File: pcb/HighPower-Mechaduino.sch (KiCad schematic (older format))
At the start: 55 parts, among them J1 SUPPLY, J2 STEPPER, P1 SWD, P4 -, P5 -, P6 -, P7 -, Q1 SSM3J328R, Q2 BSS138, SW1 B3U-1000P, U1 AS5047D, U2 AP2112K-3.3TRG1, U3 AT24CS64-SSHM, U9 LM75BD

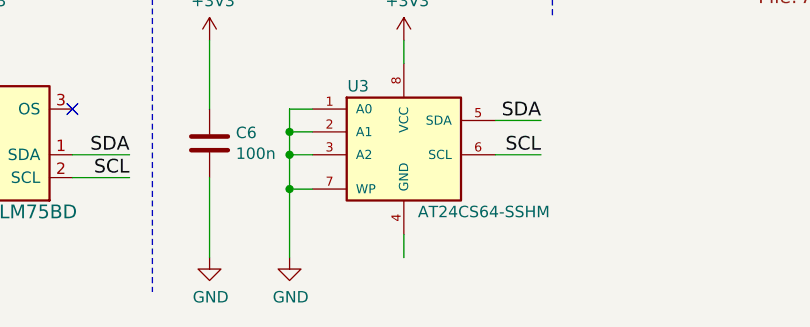
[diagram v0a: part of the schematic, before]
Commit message: Fix little schematic error
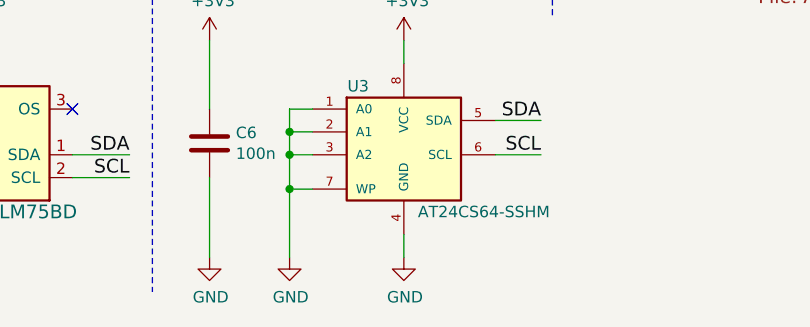
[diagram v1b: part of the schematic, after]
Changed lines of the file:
@@
 Wire Notes Line
 	4650 2700 500  2700
+$Comp
+L GND #PWR?
+U 1 1 583C420C
+P 6300 7550
+F 0 "#PWR?" H 6300 7300 50  0001 C CNN
+F 1 "GND" H 6305 7377 50  0000 C CNN
+F 2 "" H 6300 7550 50  0000 C CNN
+F 3 "" H 6300 7550 50  0000 C CNN
+	1    6300 7550
+	1    0    0    -1
+$EndComp
 $EndSCHEMATC

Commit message: update mounting hole symbol
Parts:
- removed P4, P5, P6, P7: -, Mounting_Holes_local:MountingHole_4.3x6.2mm_M4_Pad_Via, symbol CONN_01X01
- added MK1, MK2, MK3, MK4: Mounting_Hole_PAD, Mounting_Holes_local:MountingHole_4.3x6.2mm_M4_Pad_Via, symbol Mounting_Hole_PAD
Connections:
- wire segments 183 -> 215
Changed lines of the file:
@@
 AIOUT2
-$Comp
-L CONN_01X01 P4
-U 1 1 5815773D
-P 2900 2950
-F 0 "P4" V 2865 2862 50  0000 R CNN
-F 1 "-" V 2774 2862 50  0000 R CNN
-F 2 "Mounting_Holes_local:MountingHole_4.3x6.2mm_M4_Pad_Via" H 2900 2950 50  0001 C CNN
-F 3 "" H 2900 2950 50  0000 C CNN
-	1    2900 2950
-	0    -1   -1   0
-$EndComp
-$Comp
-L CONN_01X01 P5
-U 1 1 58158BF4
-P 3100 2950
-F 0 "P5" V 3065 2862 50  0000 R CNN
-F 1 "-" V 2974 2862 50  0000 R CNN
-F 2 "Mounting_Holes_local:MountingHole_4.3x6.2mm_M4_Pad_Via" H 3100 2950 50  0001 C CNN
-F 3 "" H 3100 2950 50  0000 C CNN
-	1    3100 2950
-	0    -1   -1   0
-$EndComp
-$Comp
-L CONN_01X01 P6
-U 1 1 58158DFB
-P 3300 2950
-F 0 "P6" V 3265 2862 50  0000 R CNN
-F 1 "-" V 3174 2862 50  0000 R CNN
-F 2 "Mounting_Holes_local:MountingHole_4.3x6.2mm_M4_Pad_Via" H 3300 2950 50  0001 C CNN
-F 3 "" H 3300 2950 50  0000 C CNN
-	1    3300 2950
-	0    -1   -1   0
-$EndComp
-$Comp
-L CONN_01X01 P7
-U 1 1 58159001
-P 3500 2950
-F 0 "P7" V 3465 2862 50  0000 R CNN
-F 1 "-" V 3374 2862 50  0000 R CNN
-F 2 "Mounting_Holes_local:MountingHole_4.3x6.2mm_M4_Pad_Via" H 3500 2950 50  0001 C CNN
-F 3 "" H 3500 2950 50  0000 C CNN
-	1    3500 2950
-	0    -1   -1   0
-$EndComp
 $Comp
 L GND #PWR036
 U 1 1 58159A34
-P 2900 3250
-F 0 "#PWR036" H 2900 3000 50  0001 C CNN
-F 1 "GND" H 2905 3077 50  0000 C CNN
-F 2 "" H 2900 3250 50  0000 C CNN
-F 3 "" H 2900 3250 50  0000 C CNN
-	1    2900 3250
+P 3050 3250
+F 0 "#PWR036" H 3050 3000 50  0001 C CNN
+F 1 "GND" H 3055 3077 50  0000 C CNN
+F 2 "" H 3050 3250 50  0000 C CNN
+F 3 "" H 3050 3250 50  0000 C CNN
+	1    3050 3250
 	1    0    0    -1
 $EndComp
@@
 L GND #PWR037
 U 1 1 58159EEF
-P 3100 3250
-F 0 "#PWR037" H 3100 3000 50  0001 C CNN
-F 1 "GND" H 3105 3077 50  0000 C CNN
-F 2 "" H 3100 3250 50  0000 C CNN
-F 3 "" H 3100 3250 50  0000 C CNN
-	1    3100 3250
+P 3400 3250
+F 0 "#PWR037" H 3400 3000 50  0001 C CNN
+F 1 "GND" H 3405 3077 50  0000 C CNN
+F 2 "" H 3400 3250 50  0000 C CNN
+F 3 "" H 3400 3250 50  0000 C CNN
+	1    3400 3250
 	1    0    0    -1
 $EndComp
@@
 L GND #PWR038
 U 1 1 5815A0EF
-P 3300 3250
-F 0 "#PWR038" H 3300 3000 50  0001 C CNN
-F 1 "GND" H 3305 3077 50  0000 C CNN
-F 2 "" H 3300 3250 50  0000 C CNN
-F 3 "" H 3300 3250 50  0000 C CNN
-	1    3300 3250
+P 3750 3250
+F 0 "#PWR038" H 3750 3000 50  0001 C CNN
+F 1 "GND" H 3755 3077 50  0000 C CNN
+F 2 "" H 3750 3250 50  0000 C CNN
+F 3 "" H 3750 3250 50  0000 C CNN
+	1    3750 3250
 	1    0    0    -1
 $EndComp
@@
 L GND #PWR039
 U 1 1 5815A2EF
-P 3500 3250
-F 0 "#PWR039" H 3500 3000 50  0001 C CNN
-F 1 "GND" H 3505 3077 50  0000 C CNN
-F 2 "" H 3500 3250 50  0000 C CNN
-F 3 "" H 3500 3250 50  0000 C CNN
-	1    3500 3250
+P 4100 3250
+F 0 "#PWR039" H 4100 3000 50  0001 C CNN
+F 1 "GND" H 4105 3077 50  0000 C CNN
+F 2 "" H 4100 3250 50  0000 C CNN
+F 3 "" H 4100 3250 50  0000 C CNN
+	1    4100 3250
 	1    0    0    -1
 $EndComp
@@
 	3800 800  3800 900
 Wire Wire Line
-	3700 700  3700 900
+	3700 700  3700 800
+Wire Wire Line
+	3700 800  3700 900
 Wire Wire Line
 	3700 800  3600 800
@@
 	8700 2300 8800 2300
 Wire Wire Line
-	8700 800  8700 2300
+	8700 800  8700 1000
+Wire Wire Line
+	8700 1000 8700 2300
 Wire Wire Line
 	8700 1000 8800 1000
@@
 	8600 3000 8800 3000
 Wire Wire Line
-	8600 1700 8600 3000
+	8600 1700 8600 2300
+Wire Wire Line
+	8600 2300 8600 3000
 Wire Wire Line
 	8600 1700 8800 1700
@@
 	7850 4550 7450 4550
 Wire Wire Line
-	7750 2800 8800 2800
+	7750 2800 7950 2800
+Wire Wire Line
+	7950 2800 8250 2800
+Wire Wire Line
+	8250 2800 8800 2800
 Wire Wire Line
 	7450 1500 7050 1500
@@
 	1200 4650 1200 5050
 Wire Wire Line
-	1150 4450 1300 4450
-Wire Wire Line
-	1600 4450 2650 4450
-Wire Wire Line
-	1700 4150 1700 4600
+	1150 4450 1200 4450
+Wire Wire Line
+	1200 4450 1300 4450
+Wire Wire Line
+	1600 4450 1700 4450
+Wire Wire Line
+	1700 4450 2200 4450
+Wire Wire Line
+	2200 4450 2650 4450
+Wire Wire Line
+	1700 4150 1700 4450
+Wire Wire Line
+	1700 4450 1700 4600
 Wire Wire Line
 	1700 4900 1700 5050
 Wire Wire Line
-	2650 4350 2650 4600
+	2650 4350 2650 4450
+Wire Wire Line
+	2650 4450 2650 4600
 Connection ~ 1700 4450
 Wire Wire Line
@@
 Connection ~ 2200 4450
 Wire Wire Line
-	5200 5200 5200 5500
+	5200 5200 5200 5300
+Wire Wire Line
+	5200 5300 5200 5450
+Wire Wire Line
+	5200 5450 5200 5500
 Wire Wire Line
 	5200 5800 5200 5850
@@
 	6250 5300 6400 5300
 Wire Wire Line
-	6400 5200 6400 5500
+	6400 5200 6400 5300
+Wire Wire Line
+	6400 5300 6400 5500
 Wire Wire Line
 	6400 5800 6400 5850
@@
 	900  1050 800  1050
 Wire Wire Line
-	800  1050 800  1450
+	800  1050 800  1150
+Wire Wire Line
+	800  1150 800  1250
+Wire Wire Line
+	800  1250 800  1350
+Wire Wire Line
+	800  1350 800  1450
 Wire Wire Line
 	800  1350 900  1350
@@
 	2300 900  2300 800
 Wire Wire Line
-	2300 1200 2300 1450
+	2300 1200 2300 1350
+Wire Wire Line
+	2300 1350 2300 1450
 Wire Wire Line
 	2300 1750 2300 1850
@@
 	7850 6050 7450 6050
 Wire Wire Line
-	5250 2500 5600 2500
+	5250 2500 5500 2500
+Wire Wire Line
+	5500 2500 5600 2500
 Wire Wire Line
 	5500 2500 5500 2600
@@
 	1000 6000 800  6000
 Wire Wire Line
-	800  5900 800  6200
+	800  5900 800  6000
+Wire Wire Line
+	800  6000 800  6100
+Wire Wire Line
+	800  6100 800  6200
 Wire Wire Line
 	800  6100 1000 6100
@@
 	2600 6950 2600 6750
 Wire Wire Line
-	2600 5900 2600 6350
+	2600 5900 2600 6000
+Wire Wire Line
+	2600 6000 2600 6350
 Connection ~ 2600 6000
 Wire Wire Line
 	800  7000 800  6900
 Wire Wire Line
-	800  6500 800  6600
+	800  6500 800  6550
+Wire Wire Line
+	800  6550 800  6600
 Connection ~ 800  6100
 Wire Wire Line
@@
 	5900 6900 5800 6900
 Wire Wire Line
-	5800 6900 5800 7550
+	5800 6900 5800 7000
+Wire Wire Line
+	5800 7000 5800 7100
+Wire Wire Line
+	5800 7100 5800 7250
+Wire Wire Line
+	5800 7250 5800 7550
 Wire Wire Line
 	5900 7000 5800 7000
@@
 	5450 7200 5450 7550
 Wire Wire Line
-	7750 1500 8800 1500
+	7750 1500 7950 1500
+Wire Wire Line
+	7950 1500 8250 1500
+Wire Wire Line
+	8250 1500 8800 1500
 Wire Wire Line
 	8250 1600 8250 1500
@@
 	10250 4550 10750 4550
 Wire Wire Line
-	3500 3150 3500 3250
-Wire Wire Line
-	3300 3150 3300 3250
-Wire Wire Line
-	3100 3150 3100 3250
-Wire Wire Line
-	2900 3150 2900 3250
+	4100 3100 4100 3250
+Wire Wire Line
+	3750 3100 3750 3250
+Wire Wire Line
+	3400 3100 3400 3250
+Wire Wire Line
+	3050 3100 3050 3250
 Wire Wire Line
 	2200 4450 2200 4600
@@
 	11050 3750 11050 3800
 Wire Wire Line
-	10850 3750 11050 3750
+	10850 3750 10950 3750
+Wire Wire Line
+	10950 3750 11050 3750
 Wire Wire Line
 	10850 3750 10850 3800
@@
 	3750 5050 3750 5150
 Wire Wire Line
-	3750 5450 3750 5550
+	3750 5450 3750 5500
+Wire Wire Line
+	3750 5500 3750 5550
 Wire Wire Line
 	3750 5850 3750 5950
 Wire Wire Line
-	3750 5500 4350 5500
+	3750 5500 4050 5500
+Wire Wire Line
+	4050 5500 4350 5500
 Connection ~ 3750 5500
 Wire Wire Line
@@
 	4050 7000 3950 7000
 Wire Wire Line
-	3950 7000 3950 7500
+	3950 7000 3950 7100
+Wire Wire Line
+	3950 7100 3950 7200
+Wire Wire Line
+	3950 7200 3950 7500
 Wire Wire Line
 	4050 7100 3950 7100
@@
 	4650 2700 500  2700
 $Comp
-L GND #PWR?
+L GND #PWR053
 U 1 1 583C420C
 P 6300 7550
-F 0 "#PWR?" H 6300 7300 50  0001 C CNN
+F 0 "#PWR053" H 6300 7300 50  0001 C CNN
 F 1 "GND" H 6305 7377 50  0000 C CNN
 F 2 "" H 6300 7550 50  0000 C CNN
@@
 	1    0    0    -1
 $EndComp
+$Comp
+L Mounting_Hole_PAD MK1
+U 1 1 583C5587
+P 3050 3000
+F 0 "MK1" H 3150 3005 50  0000 L CNN
+F 1 "Mounting_Hole_PAD" H 3150 2960 50  0001 L CNN
+F 2 "Mounting_Holes_local:MountingHole_4.3x6.2mm_M4_Pad_Via" H 3050 3000 60  0001 C CNN
+F 3 "" H 3050 3000 60  0001 C CNN
+	1    3050 3000
+	1    0    0    -1
+$EndComp
+$Comp
+L Mounting_Hole_PAD MK2
+U 1 1 583C88C3
+P 3400 3000
+F 0 "MK2" H 3500 3005 50  0000 L CNN
+F 1 "Mounting_Hole_PAD" H 3500 2960 50  0001 L CNN
+F 2 "Mounting_Holes_local:MountingHole_4.3x6.2mm_M4_Pad_Via" H 3400 3000 60  0001 C CNN
+F 3 "" H 3400 3000 60  0001 C CNN
+	1    3400 3000
+	1    0    0    -1
+$EndComp
+$Comp
+L Mounting_Hole_PAD MK3
+U 1 1 583C8B02
+P 3750 3000
+F 0 "MK3" H 3850 3005 50  0000 L CNN
+F 1 "Mounting_Hole_PAD" H 3850 2960 50  0001 L CNN
+F 2 "Mounting_Holes_local:MountingHole_4.3x6.2mm_M4_Pad_Via" H 3750 3000 60  0001 C CNN
+F 3 "" H 3750 3000 60  0001 C CNN
+	1    3750 3000
+	1    0    0    -1
+$EndComp
+$Comp
+L Mounting_Hole_PAD MK4
+U 1 1 583C8D4A
+P 4100 3000
+F 0 "MK4" H 4200 3005 50  0000 L CNN
+F 1 "Mounting_Hole_PAD" H 4200 2960 50  0001 L CNN
+F 2 "Mounting_Holes_local:MountingHole_4.3x6.2mm_M4_Pad_Via" H 4100 3000 60  0001 C CNN
+F 3 "" H 4100 3000 60  0001 C CNN
+	1    4100 3000
+	1    0    0    -1
+$EndComp

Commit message: Improve pcb layout
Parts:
- removed W1: SUPPLY, Measurement_Points:Measurement_Point_Round-SMD-Pad_Small, symbol TEST_1P
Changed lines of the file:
@@
 NoConn ~ 7850 6150
-$Comp
-L TEST_1P W1
-U 1 1 5816D94F
-P 1200 4150
-F 0 "W1" H 1258 4270 50  0000 L CNN
-F 1 "SUPPLY" H 1258 4179 50  0000 L CNN
-F 2 "Measurement_Points:Measurement_Point_Round-SMD-Pad_Small" H 1258 4133 50  0001 L CNN
-F 3 "" H 1400 4150 50  0000 C CNN
-	1    1200 4150
-	1    0    0    -1
-$EndComp
 $Comp
 L TEST_1P W2
@@
 	3800 800  3800 900
 Wire Wire Line
-	3700 700  3700 800
-Wire Wire Line
-	3700 800  3700 900
+	3700 700  3700 900
 Wire Wire Line
 	3700 800  3600 800
@@
 	8700 2300 8800 2300
 Wire Wire Line
-	8700 800  8700 1000
-Wire Wire Line
-	8700 1000 8700 2300
+	8700 800  8700 2300
 Wire Wire Line
 	8700 1000 8800 1000
@@
 	8600 3000 8800 3000
 Wire Wire Line
-	8600 1700 8600 2300
-Wire Wire Line
-	8600 2300 8600 3000
+	8600 1700 8600 3000
 Wire Wire Line
 	8600 1700 8800 1700
@@
 	7850 4550 7450 4550
 Wire Wire Line
-	7750 2800 7950 2800
-Wire Wire Line
-	7950 2800 8250 2800
-Wire Wire Line
-	8250 2800 8800 2800
+	7750 2800 8800 2800
 Wire Wire Line
 	7450 1500 7050 1500
@@
 	1200 4650 1200 5050
 Wire Wire Line
-	1150 4450 1200 4450
-Wire Wire Line
-	1200 4450 1300 4450
-Wire Wire Line
-	1600 4450 1700 4450
-Wire Wire Line
-	1700 4450 2200 4450
-Wire Wire Line
-	2200 4450 2650 4450
-Wire Wire Line
-	1700 4150 1700 4450
-Wire Wire Line
-	1700 4450 1700 4600
+	1600 4450 2650 4450
+Wire Wire Line
+	1700 4150 1700 4600
 Wire Wire Line
 	1700 4900 1700 5050
 Wire Wire Line
-	2650 4350 2650 4450
-Wire Wire Line
-	2650 4450 2650 4600
+	2650 4350 2650 4600
 Connection ~ 1700 4450
 Wire Wire Line
@@
 Connection ~ 2200 4450
 Wire Wire Line
-	5200 5200 5200 5300
-Wire Wire Line
-	5200 5300 5200 5450
-Wire Wire Line
-	5200 5450 5200 5500
+	5200 5200 5200 5500
 Wire Wire Line
 	5200 5800 5200 5850
@@
 	6250 5300 6400 5300
 Wire Wire Line
-	6400 5200 6400 5300
-Wire Wire Line
-	6400 5300 6400 5500
+	6400 5200 6400 5500
 Wire Wire Line
 	6400 5800 6400 5850
@@
 	900  1050 800  1050
 Wire Wire Line
-	800  1050 800  1150
-Wire Wire Line
-	800  1150 800  1250
-Wire Wire Line
-	800  1250 800  1350
-Wire Wire Line
-	800  1350 800  1450
+	800  1050 800  1450
 Wire Wire Line
 	800  1350 900  1350
@@
 	2300 900  2300 800
 Wire Wire Line
-	2300 1200 2300 1350
-Wire Wire Line
-	2300 1350 2300 1450
+	2300 1200 2300 1450
 Wire Wire Line
 	2300 1750 2300 1850
@@
 	7850 6050 7450 6050
 Wire Wire Line
-	5250 2500 5500 2500
-Wire Wire Line
-	5500 2500 5600 2500
+	5250 2500 5600 2500
 Wire Wire Line
 	5500 2500 5500 2600
@@
 	1000 6000 800  6000
 Wire Wire Line
-	800  5900 800  6000
-Wire Wire Line
-	800  6000 800  6100
-Wire Wire Line
-	800  6100 800  6200
+	800  5900 800  6200
 Wire Wire Line
 	800  6100 1000 6100
@@
 	2600 6950 2600 6750
 Wire Wire Line
-	2600 5900 2600 6000
-Wire Wire Line
-	2600 6000 2600 6350
+	2600 5900 2600 6350
 Connection ~ 2600 6000
 Wire Wire Line
 	800  7000 800  6900
 Wire Wire Line
-	800  6500 800  6550
-Wire Wire Line
-	800  6550 800  6600
+	800  6500 800  6600
 Connection ~ 800  6100
 Wire Wire Line
@@
 	5900 6900 5800 6900
 Wire Wire Line
-	5800 6900 5800 7000
-Wire Wire Line
-	5800 7000 5800 7100
-Wire Wire Line
-	5800 7100 5800 7250
-Wire Wire Line
-	5800 7250 5800 7550
+	5800 6900 5800 7550
 Wire Wire Line
 	5900 7000 5800 7000
@@
 	5450 7200 5450 7550
 Wire Wire Line
-	7750 1500 7950 1500
-Wire Wire Line
-	7950 1500 8250 1500
-Wire Wire Line
-	8250 1500 8800 1500
+	7750 1500 8800 1500
 Wire Wire Line
 	8250 1600 8250 1500
@@
 	2650 4900 2650 5050
 Wire Wire Line
-	1200 4150 1200 4450
-Connection ~ 1200 4450
-Wire Wire Line
 	10250 4850 10750 4850
 Wire Wire Line
@@
 	11050 3750 11050 3800
 Wire Wire Line
-	10850 3750 10950 3750
-Wire Wire Line
-	10950 3750 11050 3750
+	10850 3750 11050 3750
 Wire Wire Line
 	10850 3750 10850 3800
@@
 	3750 5050 3750 5150
 Wire Wire Line
-	3750 5450 3750 5500
-Wire Wire Line
-	3750 5500 3750 5550
+	3750 5450 3750 5550
 Wire Wire Line
 	3750 5850 3750 5950
 Wire Wire Line
-	3750 5500 4050 5500
-Wire Wire Line
-	4050 5500 4350 5500
+	3750 5500 4350 5500
 Connection ~ 3750 5500
 Wire Wire Line
@@
 	4050 7000 3950 7000
 Wire Wire Line
-	3950 7000 3950 7100
-Wire Wire Line
-	3950 7100 3950 7200
-Wire Wire Line
-	3950 7200 3950 7500
+	3950 7000 3950 7500
 Wire Wire Line
 	4050 7100 3950 7100
@@
 	1    0    0    -1
 $EndComp
+Wire Wire Line
+	1150 4450 1300 4450
 $EndSCHEMATC

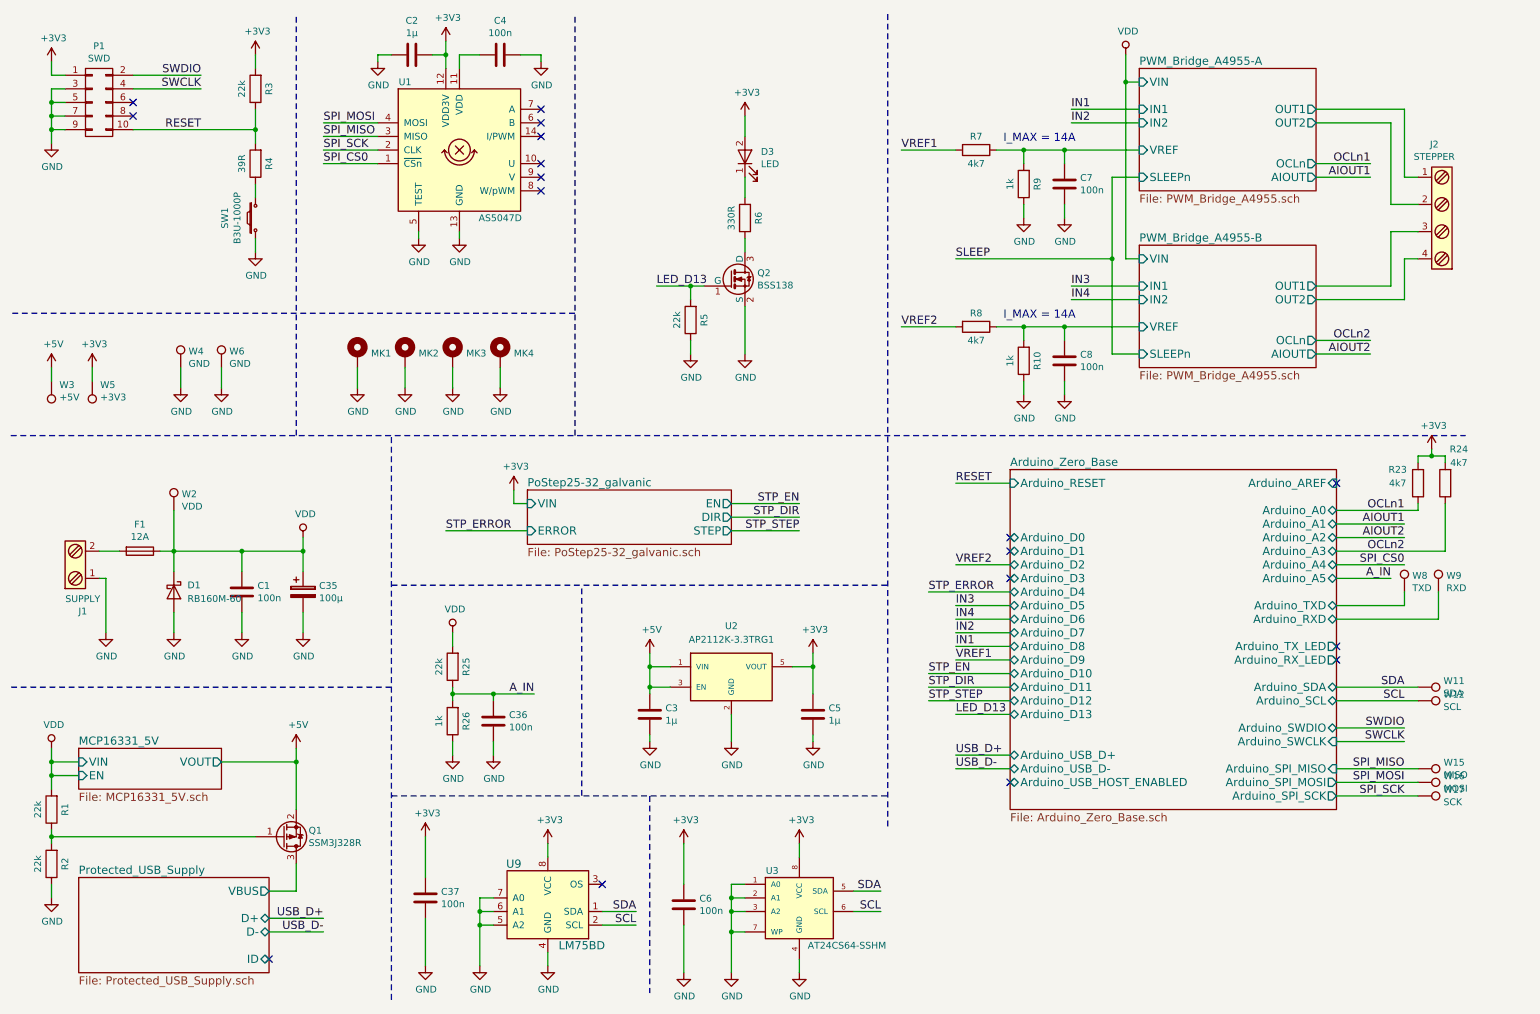
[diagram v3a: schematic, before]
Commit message: Add Digital IO connector
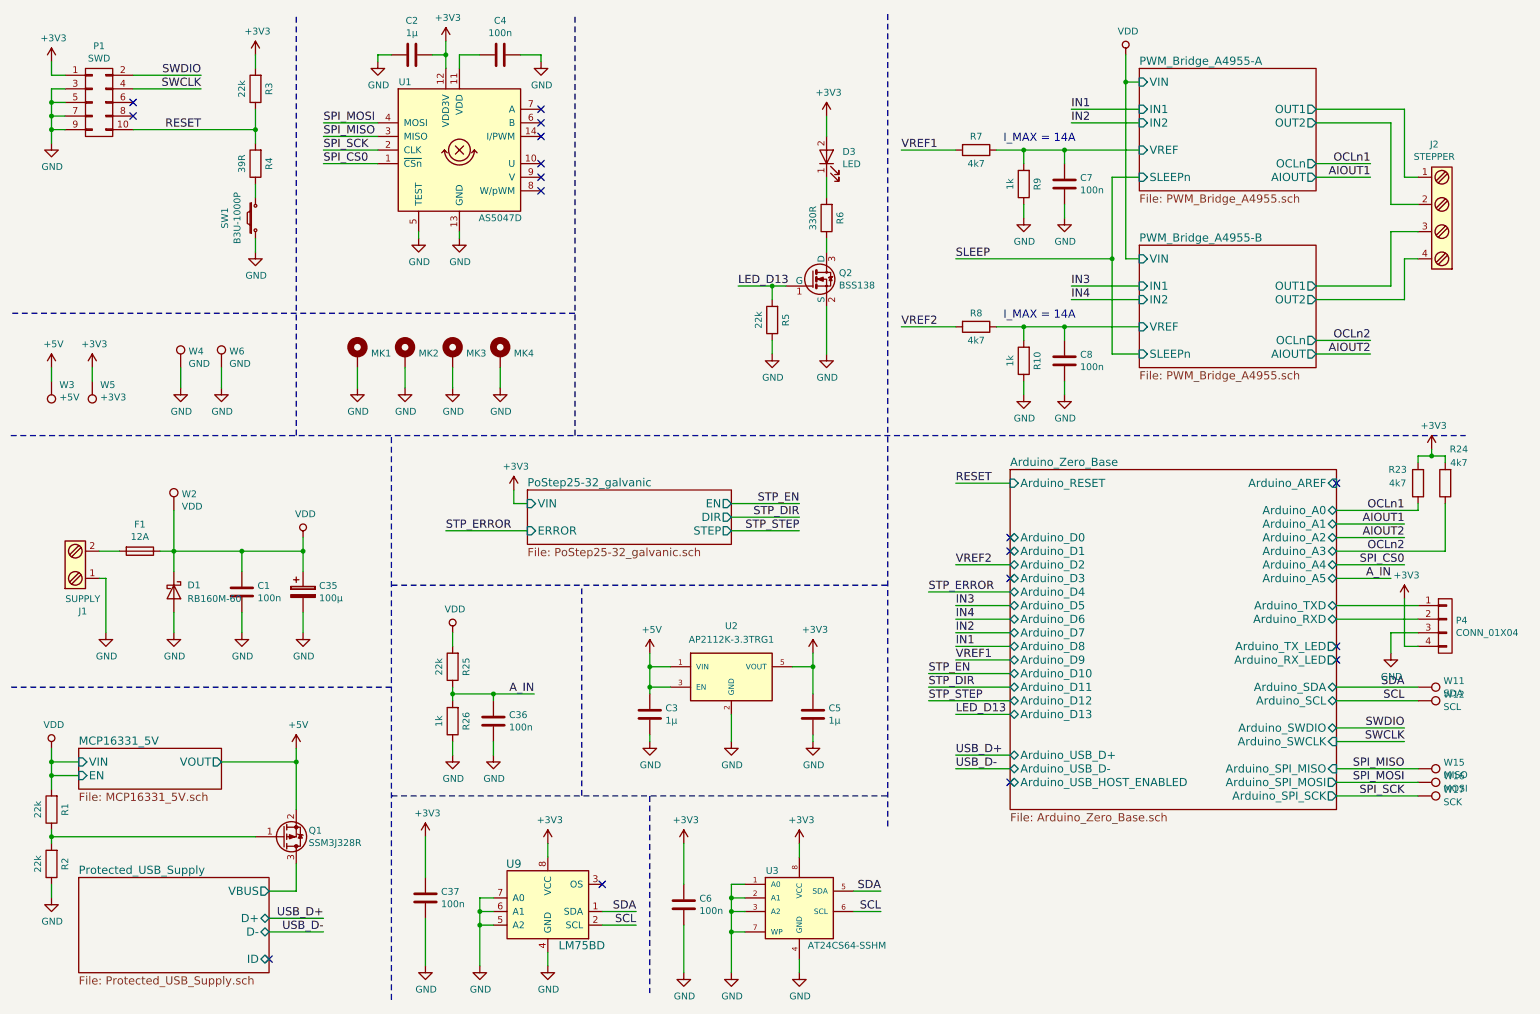
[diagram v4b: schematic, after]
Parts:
- removed W8: TXD, Measurement_Points:Measurement_Point_Round-SMD-Pad_Small, symbol TEST_1P
- removed W9: RXD, Measurement_Points:Measurement_Point_Round-SMD-Pad_Small, symbol TEST_1P
- added P4: CONN_01X04, Connectors_JST:JST_PH_B4B-PH-K_04x2.00mm_Straight, symbol CONN_01X04
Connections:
- net +3V3: now also P4.4 (P4)
- net Arduino_Zero_Base/Arduino_RXD: now also P4.2 (P2)
- net Arduino_Zero_Base/Arduino_TXD: now also P4.1 (P1)
- net GND: now also P4.3 (P3)
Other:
- moved on the sheet: D3, Q2, R5, R6
